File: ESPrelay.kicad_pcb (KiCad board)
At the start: 2 copper layers, 137.5 x 100 mm, 39 parts, among them J1 Screw_Terminal, J2 RJ45_Hanrun_HR911105A_Horizon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, J3 USB_C_Receptacle_USB2.0_14P, K1 Relay_SPDT_Latching_1coil, K2 Relay_SPDT_Latching_1coil, K3 Relay_SPDT_Latching_1coil, K4 Relay_SPDT_Latching_1coil, K5 Relay_SPDT_Latching_1coil, K6 Relay_SPDT_Latching_1coil, K7 Relay_SPDT_Latching_1coil, K8 Relay_SPDT_Latching_1coil, U1 ESP32-S3-WROOM-1, U2 ULN2803A, U3 W5500, U4 L7805, U5 LF33_TO252

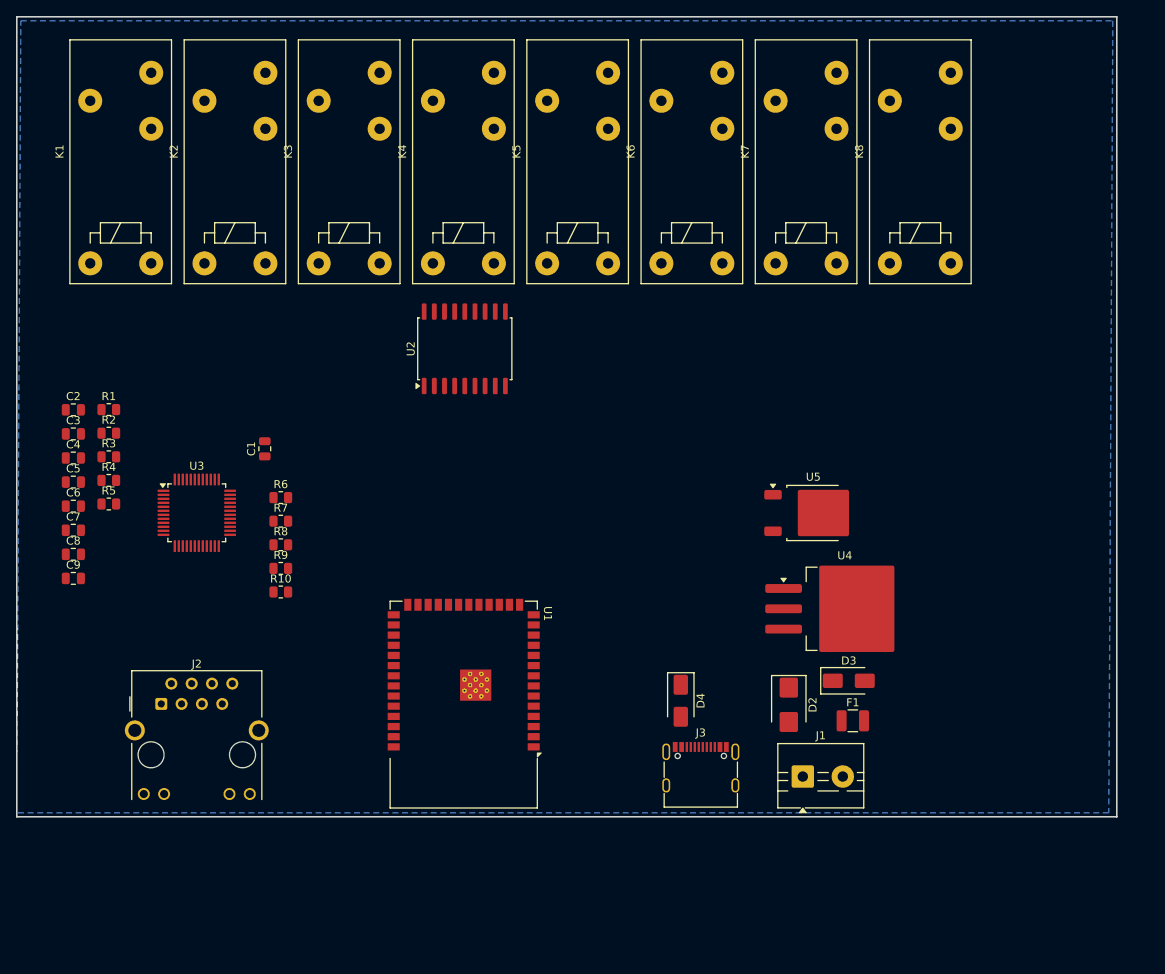
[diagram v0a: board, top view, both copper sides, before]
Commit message: avancement carte 4 relays
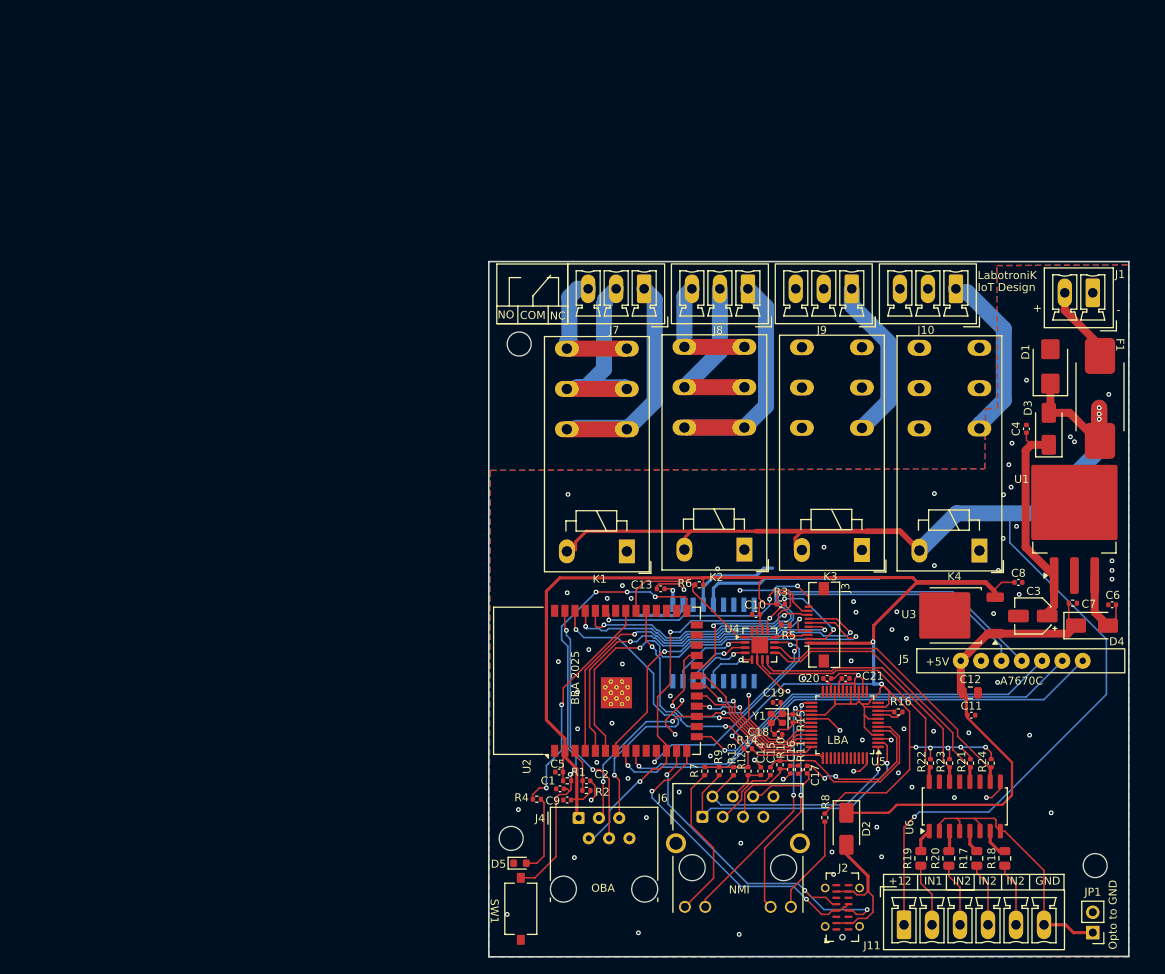
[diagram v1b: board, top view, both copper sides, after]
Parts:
- removed the C5 at (22.6, 71.2)
- removed K5, K6, K7, K8: Relay_SPDT_Latching_1coil, Relay_THT:Relay_SPDT_Schrack-RP-II-1-FormC_RM3.5mm
- removed the U2 at (71.5, 54.5)
- removed the U3 at (38.0, 75.0)
- added C1: 100nF, Capacitor_SMD:C_0402_1005Metric, F.Cu at (83.4, 109.5)
- added C10: 100nF, Capacitor_SMD:C_0402_1005Metric, F.Cu at (107.9, 87.7)
- added C11: 100nF, Capacitor_SMD:C_0402_1005Metric, F.Cu at (134.8, 100.3)
- added C12: 10µF, Capacitor_SMD:C_0805_2012Metric, F.Cu at (134.7, 97.5)
- added C13: 100nF, Capacitor_SMD:C_0402_1005Metric, F.Cu at (96.0, 84.5)
- added C14: 22nF, Capacitor_SMD:C_0402_1005Metric, F.Cu at (108.5, 107.3)
- added C15: 6.8nF, Capacitor_SMD:C_0402_1005Metric, F.Cu at (109.7, 107.3)
- added C16: 10nF, Capacitor_SMD:C_0402_1005Metric, F.Cu at (112.2, 107.1)
- added C17: 6.8nF, Capacitor_SMD:C_0402_1005Metric, F.Cu at (114.3, 107.1)
- added C18: 12pF, Capacitor_SMD:C_0402_1005Metric, F.Cu at (110.7, 102.7)
- added C19: 12pF, Capacitor_SMD:C_0402_1005Metric, F.Cu at (110.5, 98.7)
- added C20: 10nF, Capacitor_SMD:C_0402_1005Metric, F.Cu at (116.8, 95.7)
- added C21: 4.7µF - CL05A475MP5NRNC, Capacitor_SMD:C_0402_1005Metric, F.Cu at (119.1, 95.7)
- added D2: SS38, Diode_SMD:D_SMA, F.Cu at (119.2, 114.5)
- added D5: LED LTST-C193TGKT-5A, LED_SMD:LED_0603_1608Metric, F.Cu at (78.4, 118.8)
- added J10: Screw_Terminal_01x03, Connector_Phoenix_MC:PhoenixContact_MCV_1,5_3-G-3.5_1x03_P3.50mm_Vertical, F.Cu at (132.9, 47.0)
- added J11: Screw_Terminal_01x06, Connector_Phoenix_MC:PhoenixContact_MCV_1,5_6-G-3.5_1x06_P3.50mm_Vertical, F.Cu at (126.4, 126.5)
- added J4: RJ12, Connector_RJ:RJ12_Amphenol_54601-x06_Horizontal, F.Cu at (85.7, 113.2)
- added J5: A7670C MODULE, labotronik:a7670c module, F.Cu at (133.5, 93.5)
- added J6: HR911105A, Connector_RJ:RJ45_Hanrun_HR911105A_Horizontal, F.Cu at (101.2, 113.0)
- added J7: Screw_Terminal_01x03, Connector_Phoenix_MC:PhoenixContact_MCV_1,5_3-G-3.5_1x03_P3.50mm_Vertical, F.Cu at (93.9, 47.0)
- added J8: Screw_Terminal_01x03, Connector_Phoenix_MC:PhoenixContact_MCV_1,5_3-G-3.5_1x03_P3.50mm_Vertical, F.Cu at (106.9, 47.0)
- added J9: Screw_Terminal_01x03, Connector_Phoenix_MC:PhoenixContact_MCV_1,5_3-G-3.5_1x03_P3.50mm_Vertical, F.Cu at (119.9, 47.0)
- added JP1: Jumper_2_Bridged, Connector_PinHeader_2.54mm:PinHeader_1x02_P2.54mm_Vertical, F.Cu at (150.0, 127.5)
- added Q1: TBD62083AFG_EL, TBD62083AFG_EL:SOIC127P1030X245-18N, B.Cu at (102.6, 91.3)
- added R11: 49.9, Resistor_SMD:R_0402_1005Metric, F.Cu at (113.2, 107.1)
- added R12: 10, Resistor_SMD:R_0402_1005Metric, F.Cu at (106.9, 107.3)
- added R13: 49.9, Resistor_SMD:R_0402_1005Metric, F.Cu at (105.1, 107.3)
- added R14: 1k, Resistor_SMD:R_0402_1005Metric, F.Cu at (106.9, 104.5)
- added R15: 1M, Resistor_SMD:R_0402_1005Metric, F.Cu at (112.5, 100.7)
- added R16: 12.4k 1%, Resistor_SMD:R_0402_1005Metric, F.Cu at (125.7, 99.9)
- added R17: 2.2k, Resistor_SMD:R_0805_2012Metric, F.Cu at (135.5, 118.2)
- added R18: 2.2k, Resistor_SMD:R_0805_2012Metric, F.Cu at (139.0, 118.2)
- added R19: 2.2k, Resistor_SMD:R_0805_2012Metric, F.Cu at (128.5, 118.2)
- added R20: 2.2k, Resistor_SMD:R_0805_2012Metric, F.Cu at (132.0, 118.2)
- added R21: 4k7, Resistor_SMD:R_0402_1005Metric, F.Cu at (134.7, 106.3)
- added R22: 4k7, Resistor_SMD:R_0402_1005Metric, F.Cu at (129.7, 106.3)
- added R23: 4k7, Resistor_SMD:R_0402_1005Metric, F.Cu at (132.1, 106.3)
- added R24: 4k7, Resistor_SMD:R_0402_1005Metric, F.Cu at (137.3, 106.3)
- added SW1: SW_Push, Button_Switch_SMD:SW_Tactile_SPST_NO_Straight_CK_PTS636Sx25SMTRLFS, F.Cu at (78.5, 124.5)
- added U4: PCA9538BS, Package_DFN_QFN:NXP_VQFN-16-1EP_4x4mm_P0.65mm_EP2.1x2.1mm, F.Cu at (108.4, 91.5)
- added U5: W5500, Package_QFP:LQFP-48_7x7mm_P0.5mm, F.Cu at (119.0, 101.5)
- added U6: TCMT4100, Package_SO:SOP-16_4.4x10.4mm_P1.27mm, F.Cu at (134.0, 111.7)
- added Y1: X201625MOB4SI - 25Mhz, Crystal:Crystal_SMD_2016-4Pin_2.0x1.6mm, F.Cu at (110.5, 100.7)
- C2, C6: value C -> 100nF; footprint Capacitor_SMD:C_0805_2012Metric -> Capacitor_SMD:C_0402_1005Metric
- C3: value 6.8nF -> 10µF; footprint Capacitor_SMD:C_0805_2012Metric -> Capacitor_SMD:CP_Elec_4x5.4
- C4, C9: value 10nF -> 100nF; footprint Capacitor_SMD:C_0805_2012Metric -> Capacitor_SMD:C_0402_1005Metric
- C5: renamed from C1; value C -> 100nF; footprint Capacitor_SMD:C_0805_2012Metric -> Capacitor_SMD:C_0402_1005Metric
- C7: value C -> 10nF; footprint Capacitor_SMD:C_0805_2012Metric -> Resistor_SMD:R_0402_1005Metric
- C8: value 4.7µF -> 100nF; footprint Capacitor_SMD:C_0805_2012Metric -> Capacitor_SMD:C_0402_1005Metric
- D1: renamed from D2; value SM6T6V8A -> SMBJ12A
- D3: value SS38 -> B230A-13-F
- D4: value B130-E3 -> MRA4003T3G
- F1: footprint Fuse:Fuse_1210_3225Metric -> labotronik:0154250DR littelfuse 10.62 3.81
- J1: value Screw_Terminal -> POWER_INPUT; footprint TerminalBlock:TerminalBlock_MaiXu_MX126-5.0-02P_1x02_P5.00mm -> Connector_Phoenix_MC:PhoenixContact_MCV_1,5_2-G-3.5_1x02_P3.50mm_Vertical
- J2: value RJ45_Hanrun_HR911105A_Horizontal -> GT-USB-7051A; footprint Connector_RJ:RJ45_Hanrun_HR911105A_Horizontal -> Connector_USB:USB_C_Receptacle_G-Switch_GT-USB-7051x
- J3: value USB_C_Receptacle_USB2.0_14P -> LCD/BP; footprint Connector_USB:USB_C_Receptacle_G-Switch_GT-USB-7010ASV -> Connector_FFC-FPC:Molex_54548-1071_1x10-1MP_P0.5mm_Horizontal
- K1, K2, K3, K4: value Relay_SPDT_Latching_1coil -> RZ03-1C4-D012; footprint Relay_THT:Relay_SPDT_Schrack-RP-II-1-FormC_RM3.5mm -> Relay_THT:Relay_SPDT_Schrack-RT1-16A-FormC_RM5mm
- R1, R2: value 49.9 -> 10k; footprint Resistor_SMD:R_0805_2012Metric -> Resistor_SMD:R_0402_1005Metric
- R10, R9: value R -> 49.9; footprint Resistor_SMD:R_0805_2012Metric -> Resistor_SMD:R_0402_1005Metric
- R3: value 10 -> 4k7; footprint Resistor_SMD:R_0805_2012Metric -> Resistor_SMD:R_0402_1005Metric
- R4: value R -> 680; footprint Resistor_SMD:R_0805_2012Metric -> Resistor_SMD:R_0402_1005Metric
- R5: value R -> 4k7; footprint Resistor_SMD:R_0805_2012Metric -> Resistor_SMD:R_0402_1005Metric
- R6: value 1k -> 10k; footprint Resistor_SMD:R_0805_2012Metric -> Resistor_SMD:R_0402_1005Metric
- R7: value 12.4k -> 1k; footprint Resistor_SMD:R_0805_2012Metric -> Resistor_SMD:R_0402_1005Metric
- R8: value R -> 1k; footprint Resistor_SMD:R_0805_2012Metric -> Resistor_SMD:R_0402_1005Metric
- U1: renamed from U4; value L7805 -> MC7805BD2TR4G
- U2: renamed from U1; value ESP32-S3-WROOM-1 -> ESP32-S3-WROOM-1-N4
- U3: renamed from U5; value LF33_TO252 -> LF33CDT-TR
- moved C6 130.4 mm to (152.4, 86.5), turned to 180 degrees
- moved C7 125.3 mm to (147.5, 86.3)
- moved C3 122.1 mm to (142.5, 87.9), turned to 180 degrees
- moved C4 119.2 mm to (141.7, 64.5), turned to 90 degrees
- moved C8 118.2 mm to (140.7, 83.7)
- moved J2 88.9 mm to (118.7, 124.3), turned to 90 degrees
- moved R3 86.0 mm to (111.0, 86.4), turned to 180 degrees
- moved R5 85.9 mm to (111.6, 89.0), turned to 180 degrees
- moved C2 79.1 mm to (86.7, 108.5)
- moved K4 77.2 mm to (135.8, 79.7)
- moved K3 76.8 mm to (121.1, 79.7)
- moved K2 76.4 mm to (106.5, 79.6)
- moved K1 76.1 mm to (91.8, 79.8)
- moved R8 76.1 mm to (116.5, 113.1), turned to 90 degrees
- moved R2 74.6 mm to (86.7, 109.7), turned to 180 degrees
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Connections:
- C2 pad 1: GND -> Net-(U2-EN)
- C2 pad 2: /w5500/TCT -> GND
- C3 pad 1: /w5500/RXP -> Net-(D3-K)
- C3 pad 2: /w5500/RXPNET -> GND
- C4 pad 1: GND -> Net-(D3-K)
- C4 pad 2: /w5500/RCT -> GND
- C6 pad 1: GND -> Net-(D4-A)
- C6 pad 2: /w5500/XO -> GND
- C7 pad 1: GND -> +5V
- C7 pad 2: /w5500/XI -> GND
- C8 pad 1: Net-(U3-TOCAP) -> +3.3V
- C9 pad 1: Net-(U3-1V2O) -> +3.3V
- K1 pad 11: unconnected-(K1-Pad11) -> Net-(J7-Pin_2)
- K1 pad 12: unconnected-(K1-Pad12) -> Net-(J7-Pin_1)
- K1 pad 14: unconnected-(K1-Pad14) -> Net-(J7-Pin_3)
- K1 pad A1: Net-(U2-O1) -> /relais/PWR_KM1
- K2 pad 11: unconnected-(K2-Pad11) -> Net-(J8-Pin_2)
- K2 pad 12: unconnected-(K2-Pad12) -> Net-(J8-Pin_1)
- K2 pad 14: unconnected-(K2-Pad14) -> Net-(J8-Pin_3)
- K2 pad A1: Net-(U2-O2) -> /relais/PWR_KM2
- K3 pad 11: unconnected-(K3-Pad11) -> Net-(J9-Pin_2)
- K3 pad 12: unconnected-(K3-Pad12) -> Net-(J9-Pin_1)
- K3 pad 14: unconnected-(K3-Pad14) -> Net-(J9-Pin_3)
- K3 pad A1: Net-(U2-O3) -> /relais/PWR_KM3
- K4 pad 11: unconnected-(K4-Pad11) -> Net-(J10-Pin_2)
- K4 pad 12: unconnected-(K4-Pad12) -> Net-(J10-Pin_1)
- K4 pad 14: unconnected-(K4-Pad14) -> Net-(J10-Pin_3)
- K4 pad A1: Net-(U2-O4) -> /relais/PWR_KM4
- R1 pad 1: /w5500/TXP -> +3.3V
- R1 pad 2: +3.3V -> Net-(U2-IO0)
- R10 pad 1: /w5500/XO -> /w5500/RXP
- R10 pad 2: /w5500/XI -> /w5500/RCT
- R2 pad 1: /w5500/TXN -> +3.3V
- R2 pad 2: +3.3V -> Net-(U2-EN)
- R3 pad 1: /w5500/TCT -> /SDA
- R4 pad 1: +3.3V -> Net-(U2-IO40)
- R4 pad 2: Net-(J2-Pad9) -> Net-(D5-A)
- R5 pad 1: Net-(J2-Pad12) -> /SCL
- R6 pad 1: +3.3V -> /MCP_RESET
- R6 pad 2: /ETH_RESET -> +3.3V
- R7 pad 1: Net-(U3-EXRES1) -> +3.3V
- R7 pad 2: GND -> Net-(J6-Pad9)
- R8 pad 1: /w5500/RXP -> Net-(J6-Pad12)
- R8 pad 2: /w5500/RCT -> +3.3V
- R9 pad 1: /w5500/RCT -> /w5500/TXP
- R9 pad 2: /w5500/RXN -> +3.3V
- U1 pad 3: +5V -> Net-(D4-A)
- U2 pad 11: unconnected-(U1-IO18-Pad11) -> Net-(U2-IO18)
- U2 pad 12: unconnected-(U1-IO8-Pad12) -> /SDA
- U2 pad 15: unconnected-(U1-IO3-Pad15) -> /Pen
- U2 pad 17: unconnected-(U1-IO9-Pad17) -> /SCL
- U2 pad 22: unconnected-(U1-IO14-Pad22) -> /BP5
- U2 pad 27: unconnected-(U1-IO0-Pad27) -> Net-(U2-IO0)
- U2 pad 3: Net-(U1-EN) -> Net-(U2-EN)
- U2 pad 32: unconnected-(U1-IO39-Pad32) -> /MCP_RESET
- U2 pad 33: unconnected-(U1-IO40-Pad33) -> Net-(U2-IO40)
- U2 pad 35: Net-(U1-IO42) -> /COM_BP
- U2 pad 36: unconnected-(U1-RXD0-Pad36) -> /Rx
- U2 pad 37: unconnected-(U1-TXD0-Pad37) -> /Tx
- U2 pad 38: unconnected-(U1-IO2-Pad38) -> /IO2
- U2 pad 39: unconnected-(U1-IO1-Pad39) -> /IO1
- U2 pad 4: unconnected-(U1-IO4-Pad4) -> /BP1
- U2 pad 5: unconnected-(U1-IO5-Pad5) -> /BP2
- U2 pad 6: unconnected-(U1-IO6-Pad6) -> /BP3
- U2 pad 7: unconnected-(U1-IO7-Pad7) -> /BP4
- U2 pad 8: unconnected-(U1-IO15-Pad8) -> /Pwk
- U2 pad 9: unconnected-(U1-IO16-Pad9) -> /Net
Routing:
- net +3.3V: track 0.00 -> 243.5 mm, vias 0 -> 8
- net +12V: track 0.00 -> 174.6 mm, vias 0 -> 5
- net GND: track 0.00 -> 73.6 mm, vias 0 -> 78
- net /Rx: track 0.00 -> 66.7 mm, vias 0 -> 1
- net /Tx: track 0.00 -> 66.6 mm, vias 0 -> 1
- net /Pwk: track 0.00 -> 65.1 mm, vias 0 -> 1
- net /SDA: track 0.00 -> 61.4 mm, vias 0 -> 5
- net +5V: track 0.00 -> 61.1 mm
- net /Net: track 0.00 -> 60.7 mm, vias 0 -> 1
- net Net-(U2-IO0): track 0.00 -> 56.8 mm, vias 0 -> 4
- net /BP3: track 0.00 -> 54.3 mm, vias 0 -> 2
- net /Pen: track 0.00 -> 48.5 mm, vias 0 -> 1
- net /SCL: track 0.00 -> 46.7 mm, vias 0 -> 4
- net /BP4: track 0.00 -> 45.8 mm, vias 0 -> 2
- net /BP2: track 0.00 -> 45.1 mm, vias 0 -> 2
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- added copper zone on F.Cu, net GND
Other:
- board size 137.5 x 100 mm -> 80 x 86.9 mm
- board text added: "+"
- board text added: "+12"
- board text added: "+5V"
- board text added: "-"
- board text added: "A7670C"
- board text added: "BBA 2025"
- board text added: "COM"
- board text added: "GND"
- board text added: "IN1"
- board text added: "IN2"
- board text added: "IoT Design"
- board text added: "LBA"
- board text added: "LabotroniK"
- board text added: "NC"
- board text added: "NMI"
- board text added: "NO"
- board text added: "OBA"
- board text added: "Opto to GND"

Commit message: update
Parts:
- added JP2: SolderJumper_3_Bridged12, Jumper:SolderJumper-3_P1.3mm_Bridged12_RoundedPad1.0x1.5mm, F.Cu at (147.2, 103.2)
- added JP3: SolderJumper_3_Bridged12, Jumper:SolderJumper-3_P1.3mm_Bridged12_RoundedPad1.0x1.5mm, F.Cu at (147.2, 107.5)
- C21: value 4.7µF - CL05A475MP5NRNC -> 4.7µF
- D2: value SS38 -> B230A-13-F
- D4: value MRA4003T3G -> B230A-13-F
- J3: value LCD/BP -> MOLEX 545480671
- moved D2 40.0 mm to (150.0, 89.0), turned to 0 degrees
- moved D4 38.9 mm to (120.0, 114.0), turned to -90 degrees
- moved C4 17.0 mm to (140.5, 81.5), turned to 180 degrees
- moved K2 0.18 mm to (106.5, 79.8)
- moved K3 0.14 mm to (121.2, 79.8)
- moved K1 0.12 mm to (91.9, 79.8)
- moved K4 0.10 mm to (135.9, 79.8)
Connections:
- C6 pad 1: Net-(D4-A) -> Net-(D2-A)
- J2 pad A4: Net-(D2-A) -> Net-(D4-A)
- J2 pad A9: Net-(D2-A) -> Net-(D4-A)
- J2 pad B4: Net-(D2-A) -> Net-(D4-A)
- J2 pad B9: Net-(D2-A) -> Net-(D4-A)
- U1 pad 3: Net-(D4-A) -> Net-(D2-A)
- U2 pad 36: /Rx -> /Tx
- U2 pad 37: /Tx -> /Rx
- U4 pad 15: GND -> Net-(JP2-C)
- U4 pad 16: GND -> Net-(JP3-C)
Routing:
- net Net-(JP3-C): track 0.00 -> 83.5 mm, vias 0 -> 2
- net Net-(JP2-C): track 0.00 -> 68.1 mm, vias 0 -> 2
- net Net-(J10-Pin_1): track 21.8 -> 57.7 mm
- net Net-(J9-Pin_1): track 20.7 -> 56.0 mm
- net Net-(J10-Pin_2): track 0.00 -> 30.6 mm
- net Net-(J9-Pin_2): track 0.00 -> 30.0 mm
- net Net-(J10-Pin_3): track 1.37 -> 25.7 mm
- net Net-(J9-Pin_3): track 0.00 -> 22.9 mm
- net +3.3V: track 243.5 -> 265.5 mm, vias 8 -> 10
- net Net-(J8-Pin_1): track 34.4 -> 53.9 mm
- net Net-(J7-Pin_1): track 33.4 -> 52.4 mm
- net /relais/PWR_KM4: track 23.3 -> 37.3 mm
- net /relais/PWR_KM3: track 13.3 -> 25.5 mm
- net /relais/PWR_KM1: track 6.57 -> 17.9 mm
- net /relais/PWR_KM2: track 1.69 -> 12.9 mm
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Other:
- board text added: "A0"
- board text added: "A1"
- board text added: "BBA 2026"
- board text added: "DANGER"
- board text added: "DANGER HIGH VOLTAGE"
- board text added: "HIGH"
- board text added: "LabotroniK.com"
- board text added: "VOLTAGE"
- board text removed: "BBA 2025"
